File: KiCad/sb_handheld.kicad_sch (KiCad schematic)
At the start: 0 parts

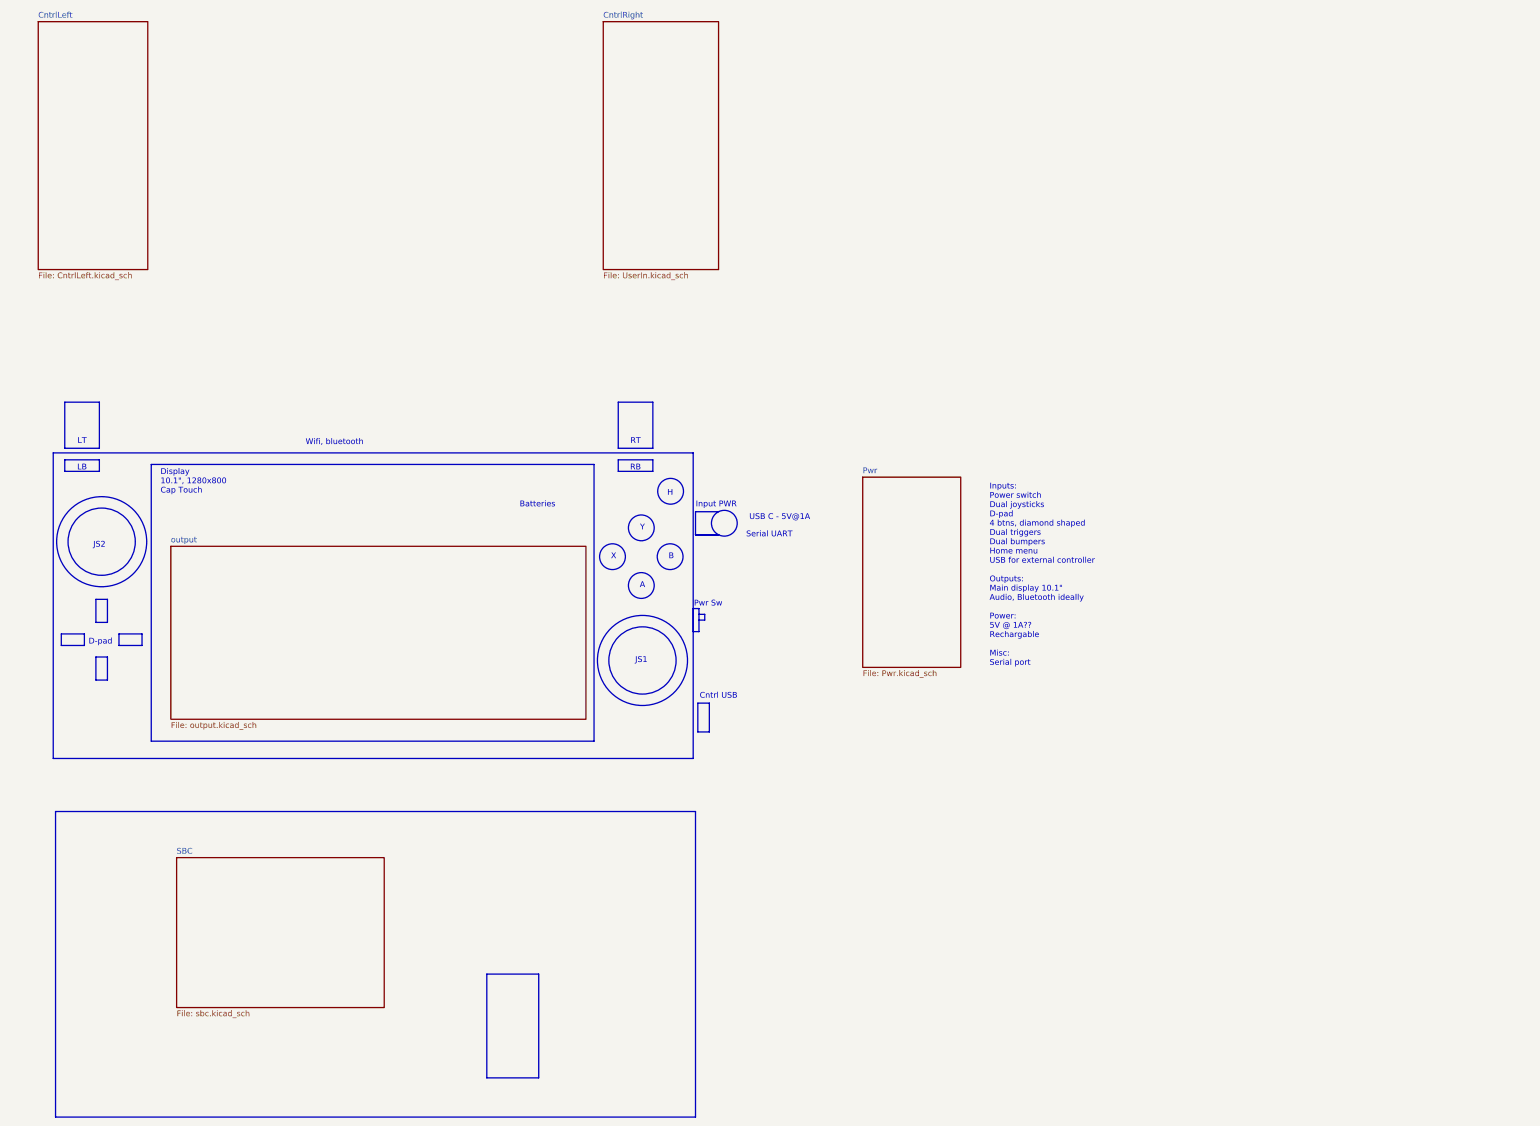
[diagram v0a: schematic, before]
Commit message: added hierachical sheets to controllers
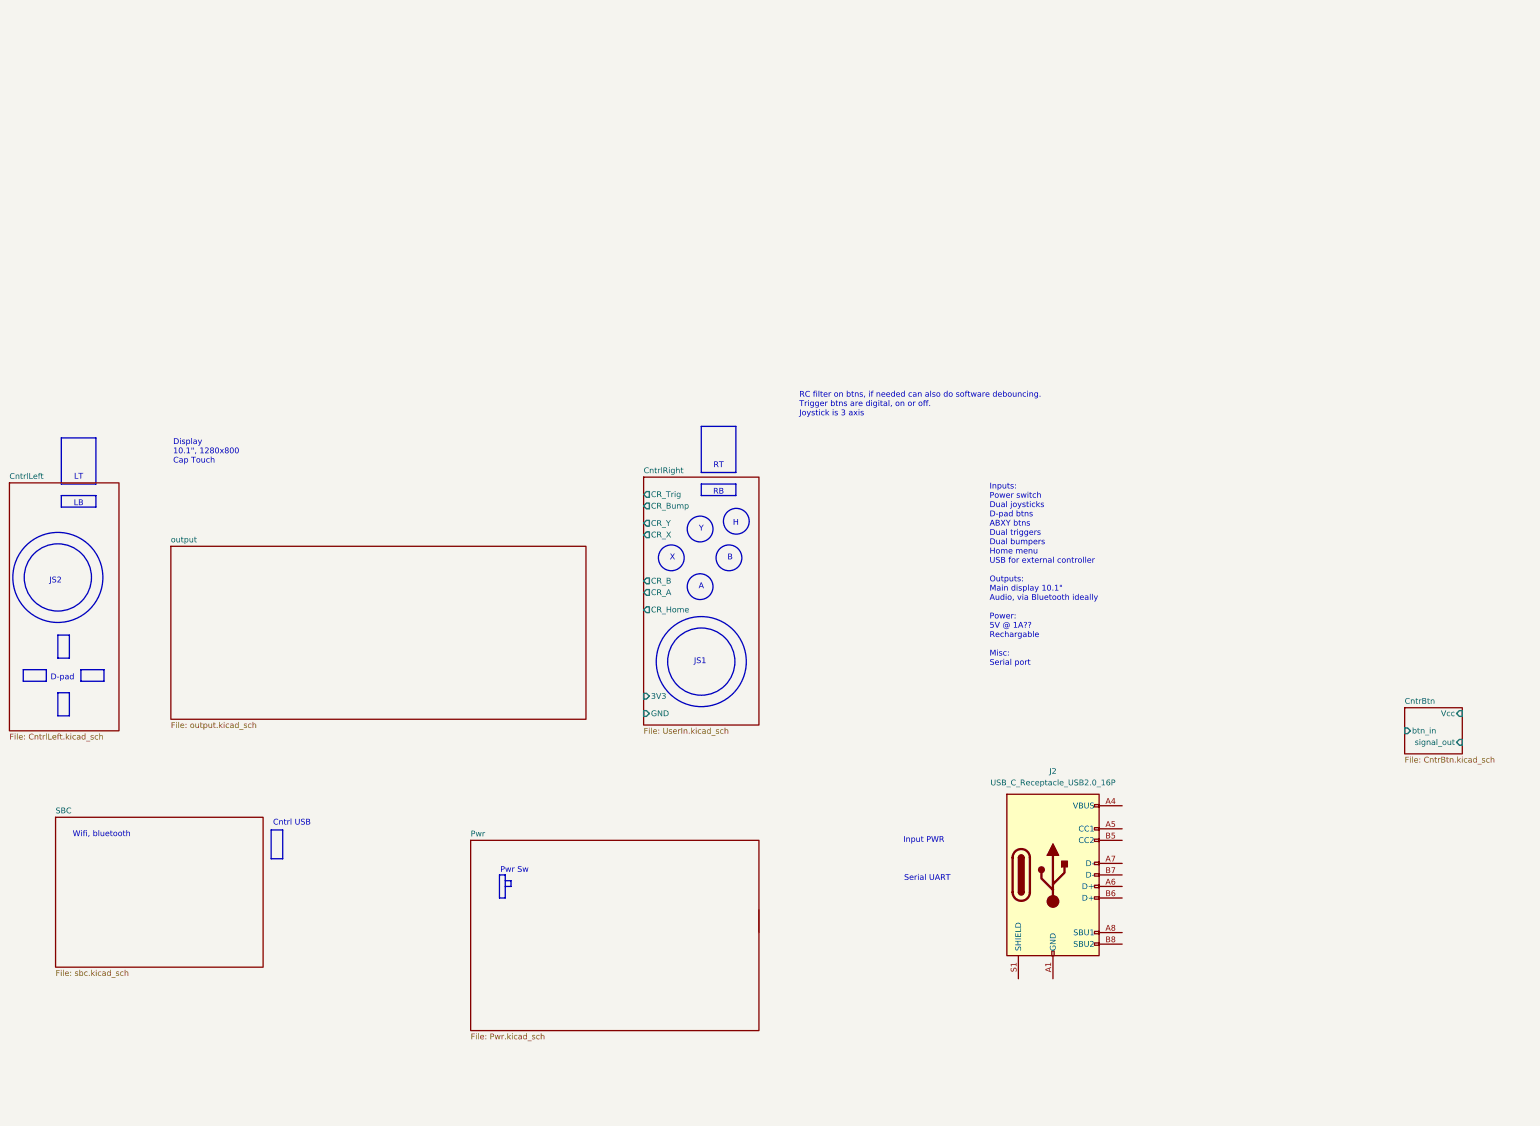
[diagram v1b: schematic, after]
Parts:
- added J2: USB_C_Receptacle_USB2.0_16P, symbol CM5_HighSpeedBreakout:USB_C_Receptacle_USB2.0_16P
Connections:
- new net: J2.A1 (GND), J2.A12 (GND), J2.B1 (GND), J2.B12 (GND)
- new net: J2.A4 (VBUS), J2.A9 (VBUS), J2.B4 (VBUS), J2.B9 (VBUS)
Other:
- added sheet CntrBtn (CntrBtn.kicad_sch)
- sheet CntrlRight ports: added 3V3, CR_A, CR_B, CR_Bump, CR_Home, CR_Trig, CR_X, CR_Y, GND; removed none
- note added: "Inputs: Power switch Dual joysticks D-pad btns ABXY btns Dual triggers Dual bumpers Home menu USB for external controller Outputs: Main display 10.1" Audio, via Bluetooth ideally Power: 5V @ 1A?? Rechargable Misc: Serial port"
- note added: "RC filter on btns, if needed can also do software debouncing. Trigger btns are digital, on or off. Joystick is 3 axis"
- note removed: "Batteries"
- note removed: "Inputs: Power switch Dual joysticks D-pad 4 btns, diamond shaped Dual triggers Dual bumpers Home menu USB for external controller Outputs: Main display 10.1" Audio, Bluetooth ideally Power: 5V @ 1A?? Rechargable Misc: Serial port"
- note removed: "USB C - 5V@1A"

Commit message: redid button pull up. Added initial joystick and display symbols
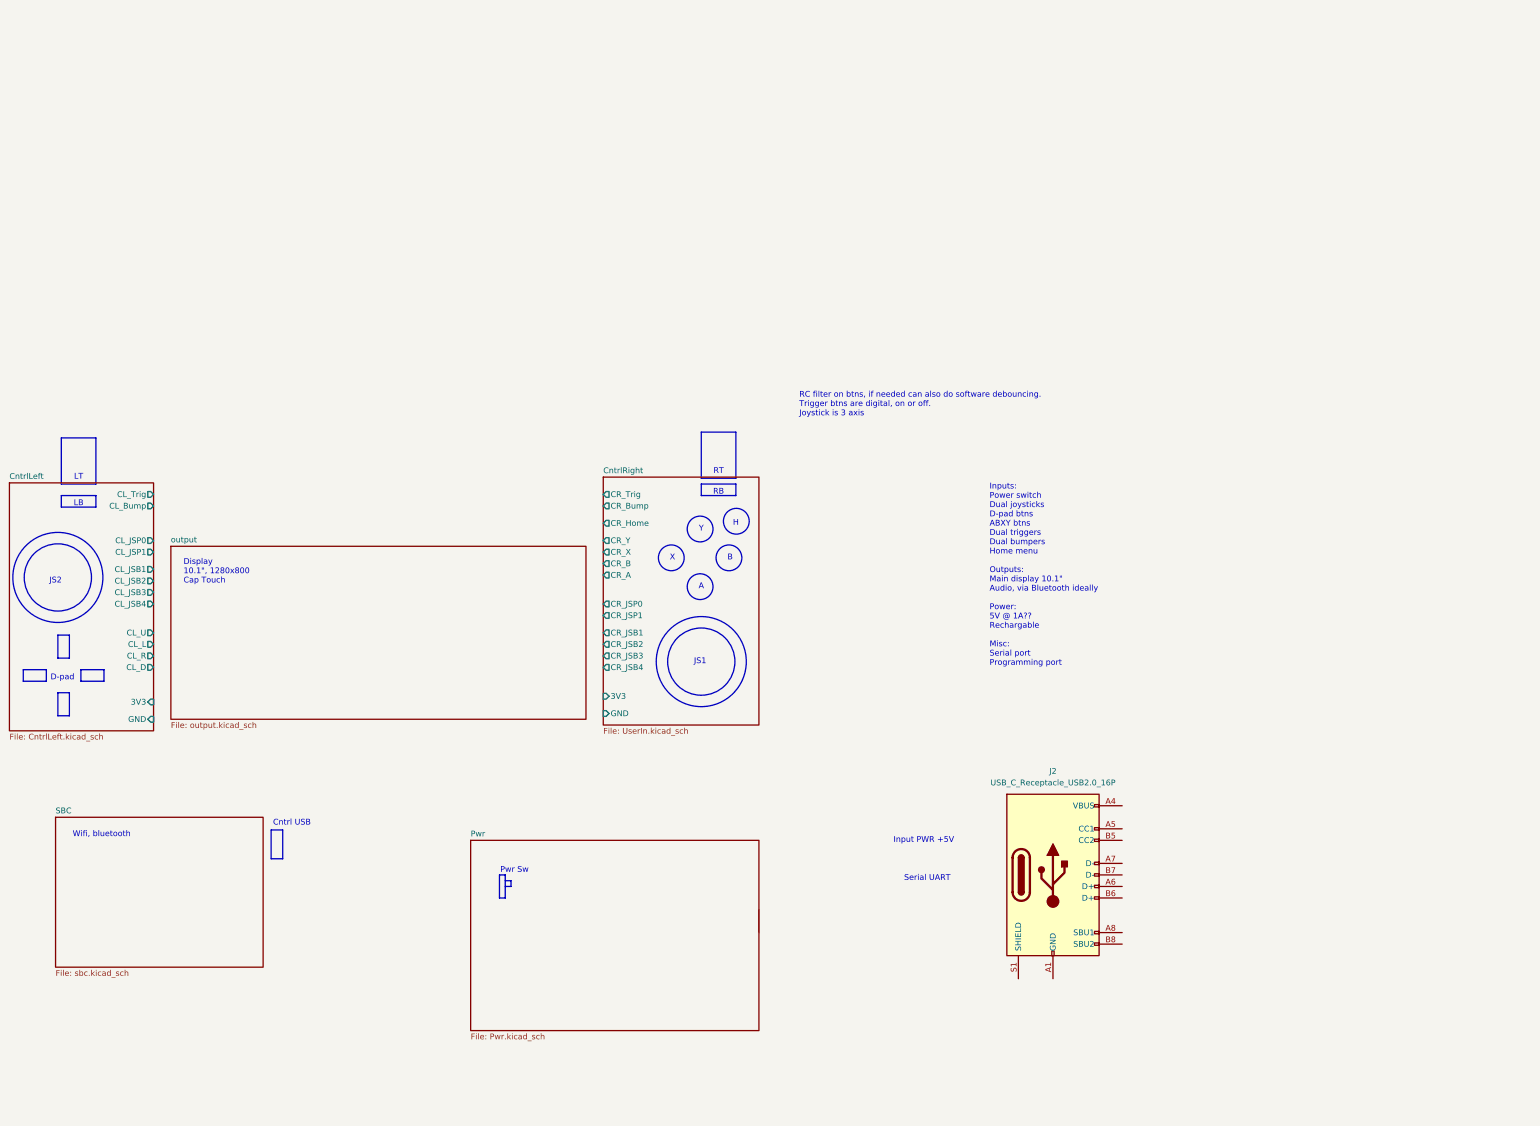
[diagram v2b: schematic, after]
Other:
- removed sheet CntrBtn
- sheet CntrlLeft ports: added 3V3, CL_Bump, CL_D, CL_JSB1, CL_JSB2, CL_JSB3, CL_JSB4, CL_JSP0, CL_JSP1, CL_L, CL_R, CL_Trig, CL_U, GND; removed none
- sheet CntrlRight ports: added CR_JSB1, CR_JSB2, CR_JSB3, CR_JSB4, CR_JSP0, CR_JSP1; removed none
- note added: "Input PWR +5V"
- note added: "Inputs: Power switch Dual joysticks D-pad btns ABXY btns Dual triggers Dual bumpers Home menu Outputs: Main display 10.1" Audio, via Bluetooth ideally Power: 5V @ 1A?? Rechargable Misc: Serial port Programming port"
- note removed: "Input PWR"
- note removed: "Inputs: Power switch Dual joysticks D-pad btns ABXY btns Dual triggers Dual bumpers Home menu USB for external controller Outputs: Main display 10.1" Audio, via Bluetooth ideally Power: 5V @ 1A?? Rechargable Misc: Serial port"
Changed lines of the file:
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@@
 	)
 	(rectangle
-		(start 172.72 26.924)
-		(end 180.34 37.084)
+		(start 172.72 28.194)
+		(end 180.34 38.354)
 		(stroke
 			(width 0)
@@
 	(text "Display\n10.1\", 1280x800\nCap Touch"
 		(exclude_from_sim no)
-		(at 56.388 32.512 0)
+		(at 58.674 58.928 0)
 		(effects
 			(font
@@
 		)
 	)
-	(text "Inputs:\nPower switch\nDual joysticks\nD-pad btns\nABXY btns\nDual triggers\nDual bumpers\nHome menu\nUSB for external controller\n\nOutputs:\nMain display 10.1\"\nAudio, via Bluetooth ideally\n\nPower:\n5V @ 1A??\nRechargable\n\nMisc:\nSerial port"
+	(text "Inputs:\nPower switch\nDual joysticks\nD-pad btns\nABXY btns\nDual triggers\nDual bumpers\nHome menu\n\nOutputs:\nMain display 10.1\"\nAudio, via Bluetooth ideally\n\nPower:\n5V @ 1A??\nRechargable\n\nMisc:\nSerial port\nProgramming port"
 		(exclude_from_sim yes)
 		(at 236.22 59.69 0)
@@
 	(text "RT"
 		(exclude_from_sim no)
-		(at 176.53 35.56 0)
+		(at 176.53 36.83 0)
 		(effects
 			(font
@@
 		)
 	)
-	(text "Input PWR"
+	(text "Input PWR +5V"
 		(exclude_from_sim no)
 		(at 221.742 118.11 0)
@@
 	(sheet
 		(at 20.32 39.37)
-		(size 24.13 54.61)
+		(size 31.75 54.61)
 		(exclude_from_sim no)
 		(in_bom yes)
@@
 			)
 		)
+		(pin "3V3" input
+			(at 52.07 87.63 0)
+			(effects
+				(font
+					(size 1.27 1.27)
+				)
+				(justify right)
+			)
+		)
+		(pin "CL_Trig" output
+			(at 52.07 41.91 0)
+			(effects
+				(font
+					(size 1.27 1.27)
+				)
+				(justify right)
+			)
+		)
+		(pin "GND" input
+			(at 52.07 91.44 0)
+			(effects
+				(font
+					(size 1.27 1.27)
+				)
+				(justify right)
+			)
+		)
+		(pin "CL_Bump" output
+			(at 52.07 44.45 0)
+			(effects
+				(font
+					(size 1.27 1.27)
+				)
+				(justify right)
+			)
+		)
+		(pin "CL_U" output
+			(at 52.07 72.39 0)
+			(effects
+				(font
+					(size 1.27 1.27)
+				)
+				(justify right)
+			)
+		)
+		(pin "CL_L" output
+			(at 52.07 74.93 0)
+			(effects
+				(font
+					(size 1.27 1.27)
+				)
+				(justify right)
+			)
+		)
+		(pin "CL_R" output
+			(at 52.07 77.47 0)
+			(effects
+				(font
+					(size 1.27 1.27)
+				)
+				(justify right)
+			)
+		)
+		(pin "CL_D" output
+			(at 52.07 80.01 0)
+			(effects
+				(font
+					(size 1.27 1.27)
+				)
+				(justify right)
+			)
+		)
+		(pin "CL_JSB3" output
+			(at 52.07 63.5 0)
+			(effects
+				(font
+					(size 1.27 1.27)
+				)
+				(justify right)
+			)
+		)
+		(pin "CL_JSB4" output
+			(at 52.07 66.04 0)
+			(effects
+				(font
+					(size 1.27 1.27)
+				)
+				(justify right)
+			)
+		)
+		(pin "CL_JSB1" output
+			(at 52.07 58.42 0)
+			(effects
+				(font
+					(size 1.27 1.27)
+				)
+				(justify right)
+			)
+		)
+		(pin "CL_JSP0" output
+			(at 52.07 52.07 0)
+			(effects
+				(font
+					(size 1.27 1.27)
+				)
+				(justify right)
+			)
+		)
+		(pin "CL_JSP1" output
+			(at 52.07 54.61 0)
+			(effects
+				(font
+					(size 1.27 1.27)
+				)
+				(justify right)
+			)
+		)
+		(pin "CL_JSB2" output
+			(at 52.07 60.96 0)
+			(effects
+				(font
+					(size 1.27 1.27)
+				)
+				(justify right)
+			)
+		)
 		(instances
 			(project "sb_handheld"
@@
 	)
 	(sheet
-		(at 160.02 38.1)
-		(size 25.4 54.61)
+		(at 151.13 38.1)
+		(size 34.29 54.61)
 		(exclude_from_sim no)
 		(in_bom yes)
@@
 		)
 		(property "Sheetname" "CntrlRight"
-			(at 160.02 37.3884 0)
+			(at 151.13 37.3884 0)
 			(effects
 				(font
@@
 		)
 		(property "Sheetfile" "UserIn.kicad_sch"
-			(at 160.02 93.2946 0)
+			(at 151.13 93.2946 0)
 			(effects
 				(font
@@
 		)
 		(pin "CR_B" output
-			(at 160.02 60.96 180)
+			(at 151.13 57.15 180)
 			(effects
 				(font
@@
 		)
 		(pin "CR_Home" output
-			(at 160.02 67.31 180)
+			(at 151.13 48.26 180)
 			(effects
 				(font
@@
 		)
 		(pin "CR_X" output
-			(at 160.02 50.8 180)
+			(at 151.13 54.61 180)
 			(effects
 				(font
@@
 		)
 		(pin "CR_Bump" output
-			(at 160.02 44.45 180)
+			(at 151.13 44.45 180)
 			(effects
 				(font
@@
 		)
 		(pin "CR_Trig" output
-			(at 160.02 41.91 180)
+			(at 151.13 41.91 180)
 			(effects
 				(font
@@
 		)
 		(pin "CR_Y" output
-			(at 160.02 48.26 180)
+			(at 151.13 52.07 180)
 			(effects
 				(font
@@
 		)
 		(pin "CR_A" output
-			(at 160.02 63.5 180)
+			(at 151.13 59.69 180)
 			(effects
 				(font
@@
 		)
 		(pin "3V3" input
-			(at 160.02 86.36 180)
+			(at 151.13 86.36 180)
 			(effects
 				(font
@@
 		)
 		(pin "GND" input
-			(at 160.02 90.17 180)
+			(at 151.13 90.17 180)
+			(effects
+				(font
+					(size 1.27 1.27)
+				)
+				(justify left)
+			)
+		)
+		(pin "CR_JSB3" output
+			(at 151.13 77.47 180)
+			(effects
+				(font
+					(size 1.27 1.27)
+				)
+				(justify left)
+			)
+		)
+		(pin "CR_JSB2" output
+			(at 151.13 74.93 180)
+			(effects
+				(font
+					(size 1.27 1.27)
+				)
+				(justify left)
+			)
+		)
+		(pin "CR_JSB4" output
+			(at 151.13 80.01 180)
+			(effects
+				(font
+					(size 1.27 1.27)
+				)
+				(justify left)
+			)
+		)
+		(pin "CR_JSB1" output
+			(at 151.13 72.39 180)
+			(effects
+				(font
+					(size 1.27 1.27)
+				)
+				(justify left)
+			)
+		)
+		(pin "CR_JSP0" output
+			(at 151.13 66.04 180)
+			(effects
+				(font
+					(size 1.27 1.27)
+				)
+				(justify left)
+			)
+		)
+		(pin "CR_JSP1" output
+			(at 151.13 68.58 180)
 			(effects
 				(font
@@
 				)
 			)
-		)
-	)
-	(sheet
-		(at 327.66 88.9)
-		(size 12.7 10.16)
-		(exclude_from_sim no)
-		(in_bom yes)
-		(on_board yes)
-		(dnp no)
-		(fields_autoplaced yes)
-		(stroke
-			(width 0.1524)
-			(type solid)
-		)
-		(fill
-			(color 0 0 0 0.0000)
-		)
-		(property "Sheetname" "CntrBtn"
-			(at 327.66 88.1884 0)
-			(effects
-				(font
-					(size 1.27 1.27)
-				)
-				(justify left bottom)
-			)
-		)
-		(property "Sheetfile" "CntrBtn.kicad_sch"
-			(at 327.66 99.6446 0)
-			(effects
-				(font
-					(size 1.27 1.27)
-				)
-				(justify left top)
-			)
-		)
-		(pin "Vcc" input
-			(at 340.36 90.17 0)
-			(effects
-				(font
-					(size 1.27 1.27)
-				)
-				(justify right)
-			)
-		)
-		(pin "btn_in" input
-			(at 327.66 93.98 180)
-			(effects
-				(font
-					(size 1.27 1.27)
-				)
-				(justify left)
-			)
-		)
-		(pin "signal_out" input
-			(at 340.36 96.52 0)
-			(effects
-				(font
-					(size 1.27 1.27)
-				)
-				(justify right)
-			)
-		)
-		(instances
-			(project "sb_handheld"
-				(path "/e2b47f54-afd4-414f-8c8f-251eedeb980e"
-					(page "7")
-				)
-			)
